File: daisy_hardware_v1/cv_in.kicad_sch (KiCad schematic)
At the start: 5 parts, among them J17 PJ398SM-12

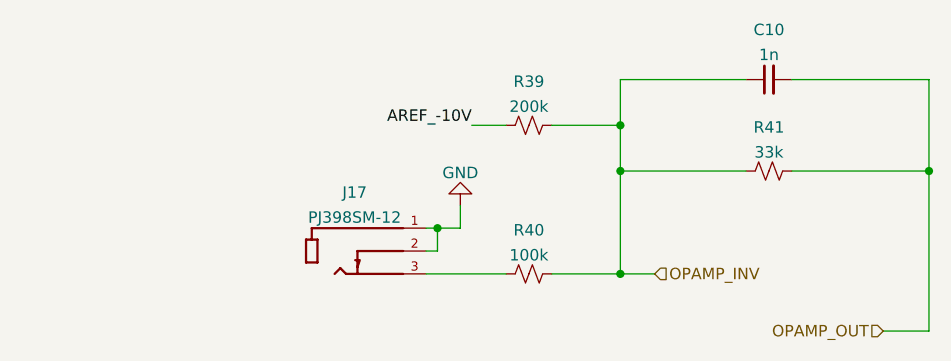
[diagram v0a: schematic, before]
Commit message: first pass of daisy schematic
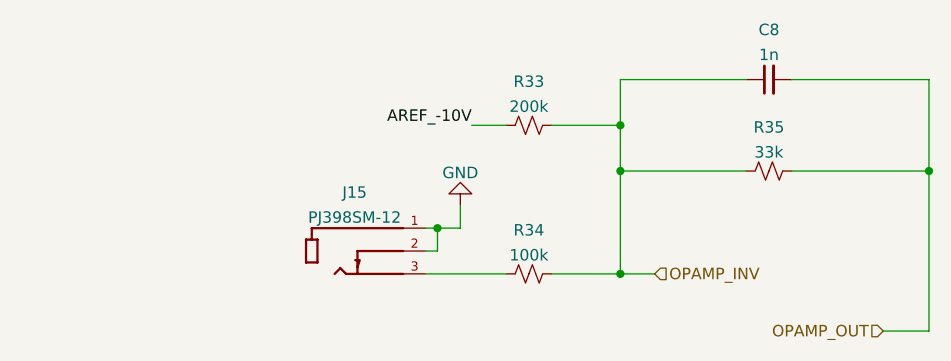
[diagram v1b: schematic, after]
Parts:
- renumbered C10 to C8, J17 to J15, R39 to R33, R40 to R34, R41 to R35
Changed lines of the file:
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@@
   (symbol (lib_id "Device:R_Small_US") (at 96.52 63.5 90)
     (in_bom yes) (on_board yes) (fields_autoplaced)
-    (property "Reference" "R39" (id 0) (at 96.52 58.6445 90))
+    (property "Reference" "R33" (id 0) (at 96.52 58.6445 90))
     (property "Value" "200k" (id 1) (at 96.52 61.4196 90))
     (property "Footprint" "" (id 2) (at 96.52 63.5 0)
@@
   (symbol (lib_id "PJ398SM-12:PJ398SM-12") (at 77.47 74.93 0)
     (in_bom yes) (on_board yes) (fields_autoplaced)
-    (property "Reference" "J17" (id 0) (at 77.1525 70.9635 0))
+    (property "Reference" "J15" (id 0) (at 77.1525 70.9635 0))
     (property "Value" "PJ398SM-12" (id 1) (at 77.1525 73.7386 0))
     (property "Footprint" "THONK_PJ398SM-12" (id 2) (at 77.47 74.93 0)
@@
   (symbol (lib_id "Device:C_Small") (at 123.19 58.42 90)
     (in_bom yes) (on_board yes) (fields_autoplaced)
-    (property "Reference" "C10" (id 0) (at 123.1963 52.8914 90))
+    (property "Reference" "C8" (id 0) (at 123.1963 52.8914 90))
     (property "Value" "1n" (id 1) (at 123.1963 55.6665 90))
     (property "Footprint" "" (id 2) (at 123.19 58.42 0)
@@
   (symbol (lib_id "power:GND") (at 88.9 72.39 180)
     (in_bom yes) (on_board yes) (fields_autoplaced)
-    (property "Reference" "#PWR0165" (id 0) (at 88.9 66.04 0)
+    (property "Reference" "#PWR0163" (id 0) (at 88.9 66.04 0)
       (effects (font (size 1.27 1.27)) hide)
     )
@@
   (symbol (lib_id "Device:R_Small_US") (at 96.52 80.01 90)
     (in_bom yes) (on_board yes) (fields_autoplaced)
-    (property "Reference" "R40" (id 0) (at 96.52 75.1545 90))
+    (property "Reference" "R34" (id 0) (at 96.52 75.1545 90))
     (property "Value" "100k" (id 1) (at 96.52 77.9296 90))
     (property "Footprint" "" (id 2) (at 96.52 80.01 0)
@@
   (symbol (lib_id "Device:R_Small_US") (at 123.19 68.58 90)
     (in_bom yes) (on_board yes) (fields_autoplaced)
-    (property "Reference" "R41" (id 0) (at 123.19 63.7245 90))
+    (property "Reference" "R35" (id 0) (at 123.19 63.7245 90))
     (property "Value" "33k" (id 1) (at 123.19 66.4996 90))
     (property "Footprint" "" (id 2) (at 123.19 68.58 0)

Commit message: Schematics coming along
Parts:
- renumbered C8 to C12, J15 to J19, R33 to R45, R34 to R46, R35 to R47
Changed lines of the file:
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@@
   (symbol (lib_id "Device:R_Small_US") (at 96.52 63.5 90)
     (in_bom yes) (on_board yes) (fields_autoplaced)
-    (property "Reference" "R33" (id 0) (at 96.52 58.6445 90))
+    (property "Reference" "R45" (id 0) (at 96.52 58.6445 90))
     (property "Value" "200k" (id 1) (at 96.52 61.4196 90))
     (property "Footprint" "" (id 2) (at 96.52 63.5 0)
@@
   (symbol (lib_id "PJ398SM-12:PJ398SM-12") (at 77.47 74.93 0)
     (in_bom yes) (on_board yes) (fields_autoplaced)
-    (property "Reference" "J15" (id 0) (at 77.1525 70.9635 0))
+    (property "Reference" "J19" (id 0) (at 77.1525 70.9635 0))
     (property "Value" "PJ398SM-12" (id 1) (at 77.1525 73.7386 0))
     (property "Footprint" "THONK_PJ398SM-12" (id 2) (at 77.47 74.93 0)
@@
   (symbol (lib_id "Device:C_Small") (at 123.19 58.42 90)
     (in_bom yes) (on_board yes) (fields_autoplaced)
-    (property "Reference" "C8" (id 0) (at 123.1963 52.8914 90))
+    (property "Reference" "C12" (id 0) (at 123.1963 52.8914 90))
     (property "Value" "1n" (id 1) (at 123.1963 55.6665 90))
     (property "Footprint" "" (id 2) (at 123.19 58.42 0)
@@
   (symbol (lib_id "power:GND") (at 88.9 72.39 180)
     (in_bom yes) (on_board yes) (fields_autoplaced)
-    (property "Reference" "#PWR0163" (id 0) (at 88.9 66.04 0)
+    (property "Reference" "#PWR0189" (id 0) (at 88.9 66.04 0)
       (effects (font (size 1.27 1.27)) hide)
     )
@@
   (symbol (lib_id "Device:R_Small_US") (at 96.52 80.01 90)
     (in_bom yes) (on_board yes) (fields_autoplaced)
-    (property "Reference" "R34" (id 0) (at 96.52 75.1545 90))
+    (property "Reference" "R46" (id 0) (at 96.52 75.1545 90))
     (property "Value" "100k" (id 1) (at 96.52 77.9296 90))
     (property "Footprint" "" (id 2) (at 96.52 80.01 0)
@@
   (symbol (lib_id "Device:R_Small_US") (at 123.19 68.58 90)
     (in_bom yes) (on_board yes) (fields_autoplaced)
-    (property "Reference" "R35" (id 0) (at 123.19 63.7245 90))
+    (property "Reference" "R47" (id 0) (at 123.19 63.7245 90))
     (property "Value" "33k" (id 1) (at 123.19 66.4996 90))
     (property "Footprint" "" (id 2) (at 123.19 68.58 0)

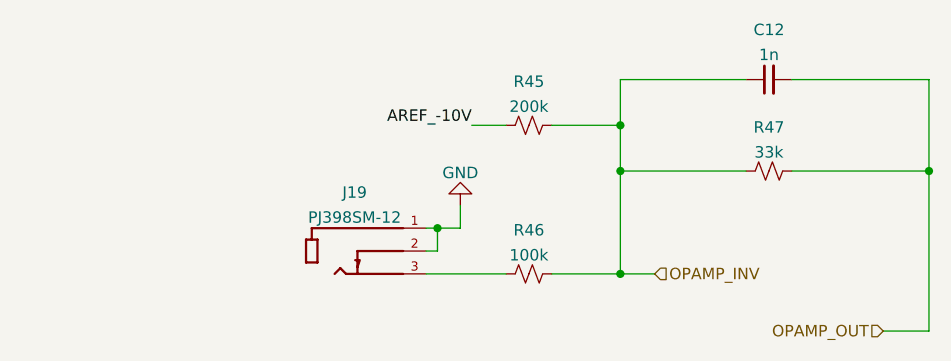
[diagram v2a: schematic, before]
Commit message: Update power + add start/end to schematics
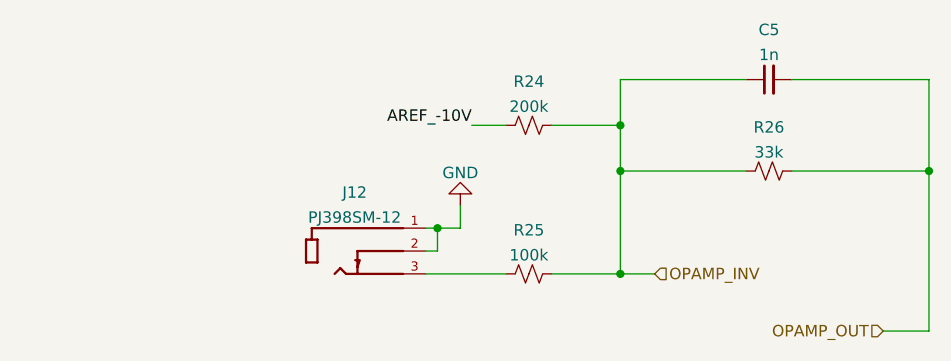
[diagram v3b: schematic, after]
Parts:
- J12: renamed from J19; footprint THONK_PJ398SM-12 -> lowstepper_internal_footprint_lib:THONK_PJ398SM-12
- renumbered C12 to C5, R45 to R24, R46 to R25, R47 to R26
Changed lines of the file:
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@@
   (junction (at 106.68 68.58) (diameter 0) (color 0 0 0 0)
+  )
+  (wire (pts (xy 85.09 80.01) (xy 93.98 80.01))
+    (stroke (width 0) (type default) (color 0 0 0 0))
   )
   (wire (pts (xy 106.68 58.42) (xy 120.65 58.42))
@@
     (stroke (width 0) (type default) (color 0 0 0 0))
   )
-  (wire (pts (xy 85.09 80.01) (xy 93.98 80.01))
-    (stroke (width 0) (type default) (color 0 0 0 0))
-  )
   (wire (pts (xy 135.89 86.36) (xy 140.97 86.36))
     (stroke (width 0) (type default) (color 0 0 0 0))
@@
   (symbol (lib_id "Device:R_Small_US") (at 96.52 63.5 90)
     (in_bom yes) (on_board yes) (fields_autoplaced)
-    (property "Reference" "R45" (id 0) (at 96.52 58.6445 90))
+    (property "Reference" "R24" (id 0) (at 96.52 58.6445 90))
     (property "Value" "200k" (id 1) (at 96.52 61.4196 90))
     (property "Footprint" "" (id 2) (at 96.52 63.5 0)
@@
   (symbol (lib_id "PJ398SM-12:PJ398SM-12") (at 77.47 74.93 0)
     (in_bom yes) (on_board yes) (fields_autoplaced)
-    (property "Reference" "J19" (id 0) (at 77.1525 70.9635 0))
+    (property "Reference" "J12" (id 0) (at 77.1525 70.9635 0))
     (property "Value" "PJ398SM-12" (id 1) (at 77.1525 73.7386 0))
-    (property "Footprint" "THONK_PJ398SM-12" (id 2) (at 77.47 74.93 0)
+    (property "Footprint" "lowstepper_internal_footprint_lib:THONK_PJ398SM-12" (id 2) (at 77.47 74.93 0)
       (effects (font (size 1.27 1.27)) (justify left bottom) hide)
     )
@@
   (symbol (lib_id "Device:C_Small") (at 123.19 58.42 90)
     (in_bom yes) (on_board yes) (fields_autoplaced)
-    (property "Reference" "C12" (id 0) (at 123.1963 52.8914 90))
+    (property "Reference" "C5" (id 0) (at 123.1963 52.8914 90))
     (property "Value" "1n" (id 1) (at 123.1963 55.6665 90))
     (property "Footprint" "" (id 2) (at 123.19 58.42 0)
@@
   (symbol (lib_id "power:GND") (at 88.9 72.39 180)
     (in_bom yes) (on_board yes) (fields_autoplaced)
-    (property "Reference" "#PWR0189" (id 0) (at 88.9 66.04 0)
+    (property "Reference" "#PWR0160" (id 0) (at 88.9 66.04 0)
       (effects (font (size 1.27 1.27)) hide)
     )
@@
   (symbol (lib_id "Device:R_Small_US") (at 96.52 80.01 90)
     (in_bom yes) (on_board yes) (fields_autoplaced)
-    (property "Reference" "R46" (id 0) (at 96.52 75.1545 90))
+    (property "Reference" "R25" (id 0) (at 96.52 75.1545 90))
     (property "Value" "100k" (id 1) (at 96.52 77.9296 90))
     (property "Footprint" "" (id 2) (at 96.52 80.01 0)
@@
   (symbol (lib_id "Device:R_Small_US") (at 123.19 68.58 90)
     (in_bom yes) (on_board yes) (fields_autoplaced)
-    (property "Reference" "R47" (id 0) (at 123.19 63.7245 90))
+    (property "Reference" "R26" (id 0) (at 123.19 63.7245 90))
     (property "Value" "33k" (id 1) (at 123.19 66.4996 90))
     (property "Footprint" "" (id 2) (at 123.19 68.58 0)

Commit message: Start splitting up board
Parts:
- C8: renamed from C5; footprint (none) -> Capacitor_SMD:C_0603_1608Metric
- R33: renamed from R24; footprint (none) -> Resistor_SMD:R_0603_1608Metric
- R34: renamed from R25; footprint (none) -> Resistor_SMD:R_0603_1608Metric
- R35: renamed from R26; footprint (none) -> Resistor_SMD:R_0603_1608Metric
- renumbered J12 to J15
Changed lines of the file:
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@@
   (symbol (lib_id "Device:R_Small_US") (at 96.52 63.5 90)
     (in_bom yes) (on_board yes) (fields_autoplaced)
-    (property "Reference" "R24" (id 0) (at 96.52 58.6445 90))
+    (property "Reference" "R33" (id 0) (at 96.52 58.6445 90))
     (property "Value" "200k" (id 1) (at 96.52 61.4196 90))
-    (property "Footprint" "" (id 2) (at 96.52 63.5 0)
+    (property "Footprint" "Resistor_SMD:R_0603_1608Metric" (id 2) (at 96.52 63.5 0)
       (effects (font (size 1.27 1.27)) hide)
     )
@@
   (symbol (lib_id "PJ398SM-12:PJ398SM-12") (at 77.47 74.93 0)
     (in_bom yes) (on_board yes) (fields_autoplaced)
-    (property "Reference" "J12" (id 0) (at 77.1525 70.9635 0))
+    (property "Reference" "J15" (id 0) (at 77.1525 70.9635 0))
     (property "Value" "PJ398SM-12" (id 1) (at 77.1525 73.7386 0))
     (property "Footprint" "lowstepper_internal_footprint_lib:THONK_PJ398SM-12" (id 2) (at 77.47 74.93 0)
@@
   (symbol (lib_id "Device:C_Small") (at 123.19 58.42 90)
     (in_bom yes) (on_board yes) (fields_autoplaced)
-    (property "Reference" "C5" (id 0) (at 123.1963 52.8914 90))
+    (property "Reference" "C8" (id 0) (at 123.1963 52.8914 90))
     (property "Value" "1n" (id 1) (at 123.1963 55.6665 90))
-    (property "Footprint" "" (id 2) (at 123.19 58.42 0)
+    (property "Footprint" "Capacitor_SMD:C_0603_1608Metric" (id 2) (at 123.19 58.42 0)
       (effects (font (size 1.27 1.27)) hide)
     )
@@
   (symbol (lib_id "power:GND") (at 88.9 72.39 180)
     (in_bom yes) (on_board yes) (fields_autoplaced)
-    (property "Reference" "#PWR0160" (id 0) (at 88.9 66.04 0)
+    (property "Reference" "#PWR0163" (id 0) (at 88.9 66.04 0)
       (effects (font (size 1.27 1.27)) hide)
     )
@@
   (symbol (lib_id "Device:R_Small_US") (at 96.52 80.01 90)
     (in_bom yes) (on_board yes) (fields_autoplaced)
-    (property "Reference" "R25" (id 0) (at 96.52 75.1545 90))
+    (property "Reference" "R34" (id 0) (at 96.52 75.1545 90))
     (property "Value" "100k" (id 1) (at 96.52 77.9296 90))
-    (property "Footprint" "" (id 2) (at 96.52 80.01 0)
+    (property "Footprint" "Resistor_SMD:R_0603_1608Metric" (id 2) (at 96.52 80.01 0)
       (effects (font (size 1.27 1.27)) hide)
     )
@@
   (symbol (lib_id "Device:R_Small_US") (at 123.19 68.58 90)
     (in_bom yes) (on_board yes) (fields_autoplaced)
-    (property "Reference" "R26" (id 0) (at 123.19 63.7245 90))
+    (property "Reference" "R35" (id 0) (at 123.19 63.7245 90))
     (property "Value" "33k" (id 1) (at 123.19 66.4996 90))
-    (property "Footprint" "" (id 2) (at 123.19 68.58 0)
+    (property "Footprint" "Resistor_SMD:R_0603_1608Metric" (id 2) (at 123.19 68.58 0)
       (effects (font (size 1.27 1.27)) hide)
     )

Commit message: Almost done PCB
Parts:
- renumbered C8 to C11, J15 to J18, R33 to R42, R34 to R43, R35 to R44
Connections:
- net JACK_BOTTOM: now reaches R43.1
- net JACK_BOTTOM: no longer J18.3
- new net JACK_TOP: J18.3
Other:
- moved on the sheet: J18
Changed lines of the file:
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@@
 (kicad_sch (version 20211123) (generator eeschema)
   (paper "A4")
-  (junction (at 86.36 74.93) (diameter 0) (color 0 0 0 0)
+  (junction (at 55.88 74.93) (diameter 0) (color 0 0 0 0)
   )
   (junction (at 106.68 63.5) (diameter 0) (color 0 0 0 0)
@@
   (junction (at 106.68 68.58) (diameter 0) (color 0 0 0 0)
   )
-  (wire (pts (xy 85.09 80.01) (xy 93.98 80.01))
-    (stroke (width 0) (type default) (color 0 0 0 0))
-  )
   (wire (pts (xy 106.68 58.42) (xy 120.65 58.42))
     (stroke (width 0) (type default) (color 0 0 0 0))
   )
   (wire (pts (xy 99.06 80.01) (xy 106.68 80.01))
+    (stroke (width 0) (type default) (color 0 0 0 0))
+  )
+  (wire (pts (xy 93.98 80.01) (xy 88.265 80.01))
     (stroke (width 0) (type default) (color 0 0 0 0))
   )
@@
     (stroke (width 0) (type default) (color 0 0 0 0))
   )
-  (wire (pts (xy 85.09 77.47) (xy 86.36 77.47))
+  (wire (pts (xy 54.61 77.47) (xy 55.88 77.47))
     (stroke (width 0) (type default) (color 0 0 0 0))
   )
@@
     (stroke (width 0) (type default) (color 0 0 0 0))
   )
-  (wire (pts (xy 85.09 74.93) (xy 86.36 74.93))
+  (wire (pts (xy 54.61 74.93) (xy 55.88 74.93))
     (stroke (width 0) (type default) (color 0 0 0 0))
   )
@@
     (stroke (width 0) (type default) (color 0 0 0 0))
   )
-  (wire (pts (xy 86.36 74.93) (xy 86.36 77.47))
+  (wire (pts (xy 55.88 74.93) (xy 55.88 77.47))
     (stroke (width 0) (type default) (color 0 0 0 0))
   )
@@
     (stroke (width 0) (type default) (color 0 0 0 0))
   )
+  (wire (pts (xy 54.61 80.01) (xy 60.325 80.01))
+    (stroke (width 0) (type default) (color 0 0 0 0))
+  )
   (wire (pts (xy 135.89 86.36) (xy 140.97 86.36))
     (stroke (width 0) (type default) (color 0 0 0 0))
   )
-  (wire (pts (xy 88.9 74.93) (xy 86.36 74.93))
+  (wire (pts (xy 58.42 74.93) (xy 55.88 74.93))
     (stroke (width 0) (type default) (color 0 0 0 0))
   )
@@
     (stroke (width 0) (type default) (color 0 0 0 0))
   )
-  (wire (pts (xy 88.9 72.39) (xy 88.9 74.93))
+  (wire (pts (xy 58.42 72.39) (xy 58.42 74.93))
     (stroke (width 0) (type default) (color 0 0 0 0))
   )
@@
     (stroke (width 0) (type default) (color 0 0 0 0))
   )
-  (label "AREF_-10V" (at 90.17 63.5 180)
-    (effects (font (size 1.27 1.27)) (justify right bottom))
+  (global_label "AREF_-10V" (shape input) (at 90.17 63.5 180) (fields_autoplaced)
+    (effects (font (size 1.27 1.27)) (justify right))
+    (property "Intersheet References" "${INTERSHEET_REFS}" (id 0) (at 77.1131 63.5794 0)
+      (effects (font (size 1.27 1.27)) (justify right) hide)
+    )
   )
   (hierarchical_label "OPAMP_INV" (shape input) (at 110.49 80.01 0)
@@
     (effects (font (size 1.27 1.27)) (justify right))
   )
+  (hierarchical_label "JACK_BOTTOM" (shape input) (at 88.265 80.01 180)
+    (effects (font (size 1.27 1.27)) (justify right))
+  )
+  (hierarchical_label "JACK_TOP" (shape input) (at 60.325 80.01 0)
+    (effects (font (size 1.27 1.27)) (justify left))
+  )
   (symbol (lib_id "Device:R_Small_US") (at 96.52 63.5 90)
     (in_bom yes) (on_board yes) (fields_autoplaced)
-    (property "Reference" "R33" (id 0) (at 96.52 58.6445 90))
+    (property "Reference" "R42" (id 0) (at 96.52 58.6445 90))
     (property "Value" "200k" (id 1) (at 96.52 61.4196 90))
     (property "Footprint" "Resistor_SMD:R_0603_1608Metric" (id 2) (at 96.52 63.5 0)
@@
     (pin "2")
   )
-  (symbol (lib_id "PJ398SM-12:PJ398SM-12") (at 77.47 74.93 0)
+  (symbol (lib_id "PJ398SM-12:PJ398SM-12") (at 46.99 74.93 0)
     (in_bom yes) (on_board yes) (fields_autoplaced)
-    (property "Reference" "J15" (id 0) (at 77.1525 70.9635 0))
-    (property "Value" "PJ398SM-12" (id 1) (at 77.1525 73.7386 0))
-    (property "Footprint" "lowstepper_internal_footprint_lib:THONK_PJ398SM-12" (id 2) (at 77.47 74.93 0)
+    (property "Reference" "J18" (id 0) (at 46.6725 70.9635 0))
+    (property "Value" "PJ398SM-12" (id 1) (at 46.6725 73.7386 0))
+    (property "Footprint" "lowstepper_internal_footprint_lib:THONK_PJ398SM-12" (id 2) (at 46.99 74.93 0)
       (effects (font (size 1.27 1.27)) (justify left bottom) hide)
     )
-    (property "Datasheet" "" (id 3) (at 77.47 74.93 0)
+    (property "Datasheet" "" (id 3) (at 46.99 74.93 0)
       (effects (font (size 1.27 1.27)) (justify left bottom) hide)
     )
-    (property "MAXIMUM_PACKAGE_HEIGHT" "14.5 mm" (id 4) (at 77.47 74.93 0)
+    (property "MAXIMUM_PACKAGE_HEIGHT" "14.5 mm" (id 4) (at 46.99 74.93 0)
       (effects (font (size 1.27 1.27)) (justify left bottom) hide)
     )
-    (property "MANUFACTURER" "Thonk" (id 5) (at 77.47 74.93 0)
+    (property "MANUFACTURER" "Thonk" (id 5) (at 46.99 74.93 0)
       (effects (font (size 1.27 1.27)) (justify left bottom) hide)
     )
-    (property "PARTREV" "1" (id 6) (at 77.47 74.93 0)
+    (property "PARTREV" "1" (id 6) (at 46.99 74.93 0)
       (effects (font (size 1.27 1.27)) (justify left bottom) hide)
     )
-    (property "STANDARD" "Manufacturer Recommendations" (id 7) (at 77.47 74.93 0)
+    (property "STANDARD" "Manufacturer Recommendations" (id 7) (at 46.99 74.93 0)
       (effects (font (size 1.27 1.27)) (justify left bottom) hide)
     )
@@
   (symbol (lib_id "Device:C_Small") (at 123.19 58.42 90)
     (in_bom yes) (on_board yes) (fields_autoplaced)
-    (property "Reference" "C8" (id 0) (at 123.1963 52.8914 90))
+    (property "Reference" "C11" (id 0) (at 123.1963 52.8914 90))
     (property "Value" "1n" (id 1) (at 123.1963 55.6665 90))
     (property "Footprint" "Capacitor_SMD:C_0603_1608Metric" (id 2) (at 123.19 58.42 0)
@@
     (pin "2")
   )
-  (symbol (lib_id "power:GND") (at 88.9 72.39 180)
-    (in_bom yes) (on_board yes) (fields_autoplaced)
-    (property "Reference" "#PWR0163" (id 0) (at 88.9 66.04 0)
+  (symbol (lib_id "power:GND") (at 58.42 72.39 180)
+    (in_bom yes) (on_board yes)
+    (property "Reference" "#PWR0188" (id 0) (at 58.42 66.04 0)
       (effects (font (size 1.27 1.27)) hide)
     )
-    (property "Value" "GND" (id 1) (at 88.9 68.7855 0))
-    (property "Footprint" "" (id 2) (at 88.9 72.39 0)
+    (property "Value" "GND" (id 1) (at 58.42 68.7855 0))
+    (property "Footprint" "" (id 2) (at 58.42 72.39 0)
       (effects (font (size 1.27 1.27)) hide)
     )
-    (property "Datasheet" "" (id 3) (at 88.9 72.39 0)
+    (property "Datasheet" "" (id 3) (at 58.42 72.39 0)
       (effects (font (size 1.27 1.27)) hide)
     )
@@
   (symbol (lib_id "Device:R_Small_US") (at 96.52 80.01 90)
     (in_bom yes) (on_board yes) (fields_autoplaced)
-    (property "Reference" "R34" (id 0) (at 96.52 75.1545 90))
+    (property "Reference" "R43" (id 0) (at 96.52 75.1545 90))
     (property "Value" "100k" (id 1) (at 96.52 77.9296 90))
     (property "Footprint" "Resistor_SMD:R_0603_1608Metric" (id 2) (at 96.52 80.01 0)
@@
   (symbol (lib_id "Device:R_Small_US") (at 123.19 68.58 90)
     (in_bom yes) (on_board yes) (fields_autoplaced)
-    (property "Reference" "R35" (id 0) (at 123.19 63.7245 90))
+    (property "Reference" "R44" (id 0) (at 123.19 63.7245 90))
     (property "Value" "33k" (id 1) (at 123.19 66.4996 90))
     (property "Footprint" "Resistor_SMD:R_0603_1608Metric" (id 2) (at 123.19 68.58 0)
